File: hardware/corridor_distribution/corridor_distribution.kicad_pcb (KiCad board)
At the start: 2 copper layers, 60 x 100 mm, 78 parts, among them CN1 C_Pack04_Split, CN2 C_Pack04_Split, J1 Screw_Terminal_01x06, J10 Screw_Terminal_01x04, J12 Conn_02x03_Odd_Even, J2 Screw_Terminal_01x06, J3 Screw_Terminal_01x06, J4 Screw_Terminal_01x06, J5 Screw_Terminal_01x06, J6 Screw_Terminal_01x06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

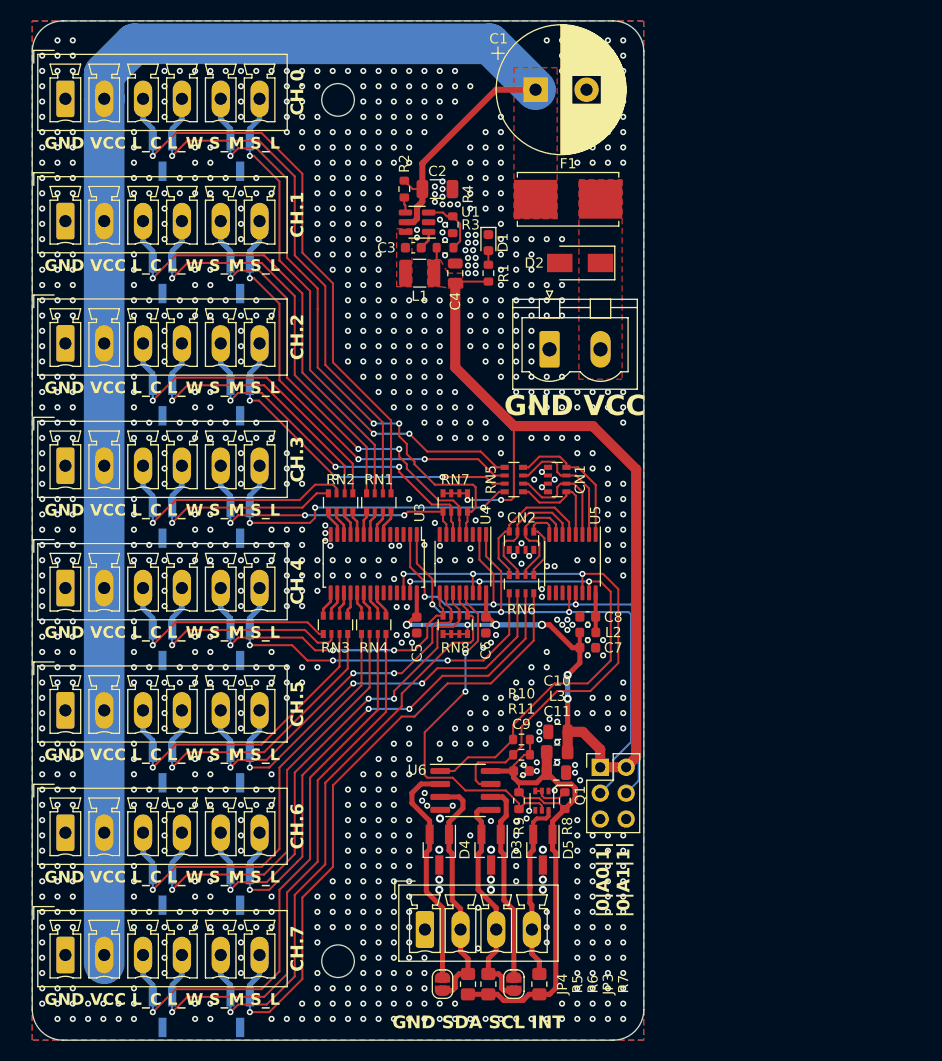
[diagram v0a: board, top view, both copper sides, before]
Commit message: led balance and corridor ready
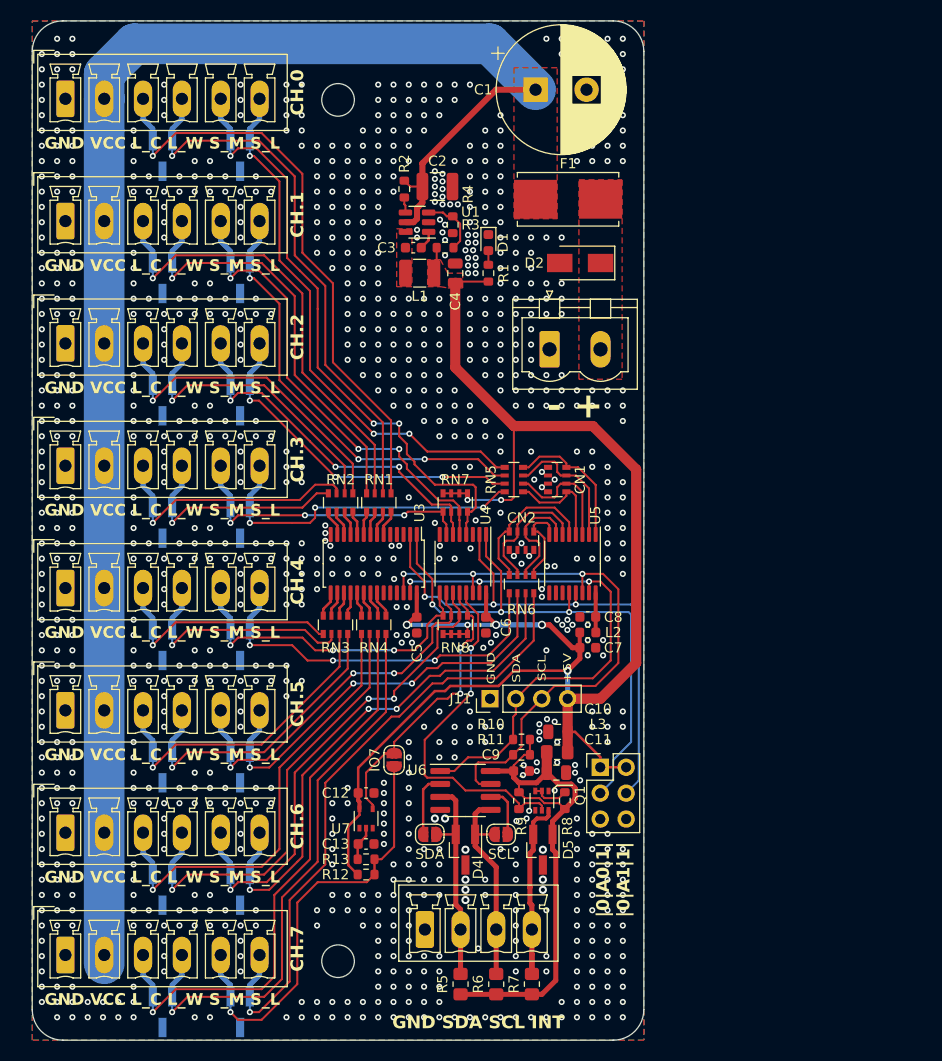
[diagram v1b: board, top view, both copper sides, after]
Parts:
- removed D3: D, Package_TO_SOT_SMD:SOT-23_Handsoldering
- added C12: 100n 50V, Capacitor_SMD:C_0603_1608Metric, F.Cu at (188.5, 104.2)
- added C13: 100n 50V, Capacitor_SMD:C_0603_1608Metric, F.Cu at (188.5, 109.2)
- added J11: Conn_01x04, Connector_PinHeader_2.54mm:PinHeader_1x04_P2.54mm_Vertical, F.Cu at (200.7, 95.0)
- added JP1: IO7, Jumper:SolderJumper-2_P1.3mm_Open_RoundedPad1.0x1.5mm, F.Cu at (191.2, 101.0)
- added R12: 4.7k, Resistor_SMD:R_0603_1608Metric, F.Cu at (188.5, 112.2)
- added R13: 100k, Resistor_SMD:R_0603_1608Metric, F.Cu at (188.5, 110.8)
- added U7: 74LVC1G17, Package_TO_SOT_SMD:SOT-353_SC-70-5, F.Cu at (188.5, 106.8)
- C1: value C_Polarized -> 1000uF 50V D12.5xL25mm
- C10, C11, C4: value 22u -> 22u 10V
- C2: value 10u -> 10u 50V; footprint Capacitor_SMD:C_1206_3216Metric -> Capacitor_SMD:C_1210_3225Metric
- C3, C9: value 100n -> 100n 50V
- C5, C6, C7, C8: value C -> 100n 50V
- CN1, CN2: value C_Pack04_Split -> 100n 50V
- D1: value LED -> green LED
- D10, D11, D12, D13, D14, D15, D16, D17, D18, D19, D20, D21, D4, D5, D6, D7, D8, D9: value D -> SM05
- D2: value D_Zener -> SMAJ36A
- F1: value Fuse -> 01550900M
- JP3: value SolderJumper_2_Open -> SCL
- JP4: value SolderJumper_2_Open -> SDA
- L1: value 22u -> CBC3225T220KR
- L2: value FerriteBead -> BLM18BD252SN1D
- L3: value FerriteBead -> MMZ2012R102AT000
- Q1: value Q_Dual_NMOS_S1G1D2S2G2D1 -> DMN2004DWK
- R1: value R -> 2.2k
- R10, R11: value 4k7 -> 4.7k
- R3: value 52k5 -> 105k 0.5%
- R4: value 10k -> 20k 0.5%
- RN1, RN2, RN3, RN4: value R_Pack04 -> 100
- RN5, RN6: value R_Pack04_Split -> 68k
- RN7, RN8: value R_Pack04_Split -> 4.7k
- U1: value TD1465 -> TD1469
- U4: value TCA9554PW -> TCA9554APW
- moved JP3 14.7 mm to (201.8, 108.3), turned to 180 degrees
- moved JP4 14.7 mm to (194.8, 108.3), turned to 0 degrees
- moved D4 2.56 mm to (198.2, 109.8)
- moved R6 0.77 mm to (201.3, 123.0)
- moved R5 0.73 mm to (197.8, 123.0)
- moved R7 0.73 mm to (204.8, 123.0)
- moved C2 0.25 mm to (195.5, 44.8)
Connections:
- D4 pad 1: /bus_in/SDA_{T} -> /bus_in/SCL_{T}
- D4 pad 2: /bus_in/SDA_{R} -> /bus_in/SDA_{T}
- RN8 pad 5: /IO/IO7 -> /IO/IO7S
- U4 pad 12: /IO/IO7 -> /IO/IO7S
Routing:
- net +5V: track 129.6 -> 162.6 mm, vias 8 -> 7
- net /IO/IO7S: track 0.00 -> 28.3 mm, vias 0 -> 2
- net /IO/IO7: track 60.5 -> 42.8 mm
- net /bus_in/SDA_{R}: track 22.8 -> 6.31 mm
- net /bus_in/SCL_{R}: track 19.8 -> 5.05 mm
- net /bus_in/SDA_{T}: track 24.5 -> 20.8 mm
- net /IO/IO7F: track 0.00 -> 3.39 mm
- net /bus_in/SCL_{T}: track 22.5 -> 20.1 mm
- net /bus_in/INT: track 17.7 -> 19.4 mm
- net /SDA: track 52.2 -> 53.6 mm
- net GND: vias 1059 -> 980
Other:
- board text added: "- +"
- board text added: "GND SDA SCL +5V"
- board text removed: "GND VCC"

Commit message: various
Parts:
- added C14: 100n 50V, Capacitor_SMD:C_0603_1608Metric, F.Cu at (227.7, 81.4)
- added C15: 100n 50V, Capacitor_SMD:C_0603_1608Metric, F.Cu at (241.2, 86.5)
- added JP2: SolderJumper_2_Open, Jumper:SolderJumper-2_P1.3mm_Open_RoundedPad1.0x1.5mm, F.Cu at (233.8, 77.7)
- added JP5: SolderJumper_2_Open, Jumper:SolderJumper-2_P1.3mm_Open_RoundedPad1.0x1.5mm, F.Cu at (233.8, 81.2)
- added JP6: SolderJumper_2_Open, Jumper:SolderJumper-2_P1.3mm_Open_RoundedPad1.0x1.5mm, F.Cu at (241.4, 83.5)
- added R14: 330, Resistor_SMD:R_0603_1608Metric_Pad0.98x0.95mm_HandSolder, F.Cu at (223.6, 87.2)
- added R15: 330, Resistor_SMD:R_0603_1608Metric_Pad0.98x0.95mm_HandSolder, F.Cu at (223.5, 89.8)
- added R16: R, Resistor_SMD:R_1210_3225Metric_Pad1.30x2.65mm_HandSolder, F.Cu at (224.4, 78.0)
- added R17: R, Resistor_SMD:R_0603_1608Metric_Pad0.98x0.95mm_HandSolder, F.Cu at (228.8, 69.8)
- added U9: INA190, Package_TO_SOT_SMD:SOT-363_SC-70-6, F.Cu at (223.5, 82.1)
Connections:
- D21 pad 1: /nodes/PW14 -> /nodes/node conn 7/LED_C
- D21 pad 2: /nodes/PW15 -> /nodes/node conn 7/LED_W
- F1 pad 1: +36V -> Net-(U9-+)
- J8 pad 3: /nodes/PW14 -> /nodes/node conn 7/LED_C
- J8 pad 4: /nodes/PW15 -> /nodes/node conn 7/LED_W
- U3 pad 25: GND -> Net-(JP2-B)
- U5 pad 10: unconnected-(U5-REFin/REFout-Pad10) -> /ADC/REF
- U5 pad 11: unconnected-(U5-COM-Pad11) -> GND
